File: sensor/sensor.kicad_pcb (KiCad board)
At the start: 2 copper layers, 34 x 34 mm, 17 parts

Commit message: Thubmstick v1
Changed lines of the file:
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@@
       (effects (font (size 1 1) (thickness 0.15)))
     )
-    (fp_rect (start -4.55 -8.1) (end 4.55 8.1) (layer "F.SilkS") (width 0.12) (fill none))
+    (fp_rect (start -4.55 -8.1) (end 4.55 8.1) (layer "Edge.Cuts") (width 0.12) (fill none))
     (pad "1" thru_hole circle (at -5.35 -6.58) (size 1.2 1.2) (drill 0.7) (layers *.Cu *.Mask)
       (net 11 "unconnected-(SN1-Pad1)") (pinfunction "NC") (pintype "input+no_connect"))
@@
     (pad "16" thru_hole circle (at 5.35 -5.69) (size 1.2 1.2) (drill 0.7) (layers *.Cu *.Mask)
       (net 17 "unconnected-(SN1-Pad16)") (pinfunction "NC") (pintype "input+no_connect"))
-    (zone (net 0) (net_name "") (layer "F.SilkS") (hatch edge 0.508)
-      (connect_pads (clearance 0))
-      (min_thickness 0.254)
-      (keepout (tracks not_allowed) (vias not_allowed) (pads not_allowed ) (copperpour allowed) (footprints allowed))
-      (fill (thermal_gap 0.508) (thermal_bridge_width 0.508))
-      (polygon
-        (pts
-          (xy 154.55 108.1)
-          (xy 145.45 108.1)
-          (xy 145.45 91.9)
-          (xy 154.55 91.9)
-        )
-      )
-    )
   )
   (footprint "Capacitor_SMD:C_0603_1608Metric" (layer "F.Cu")

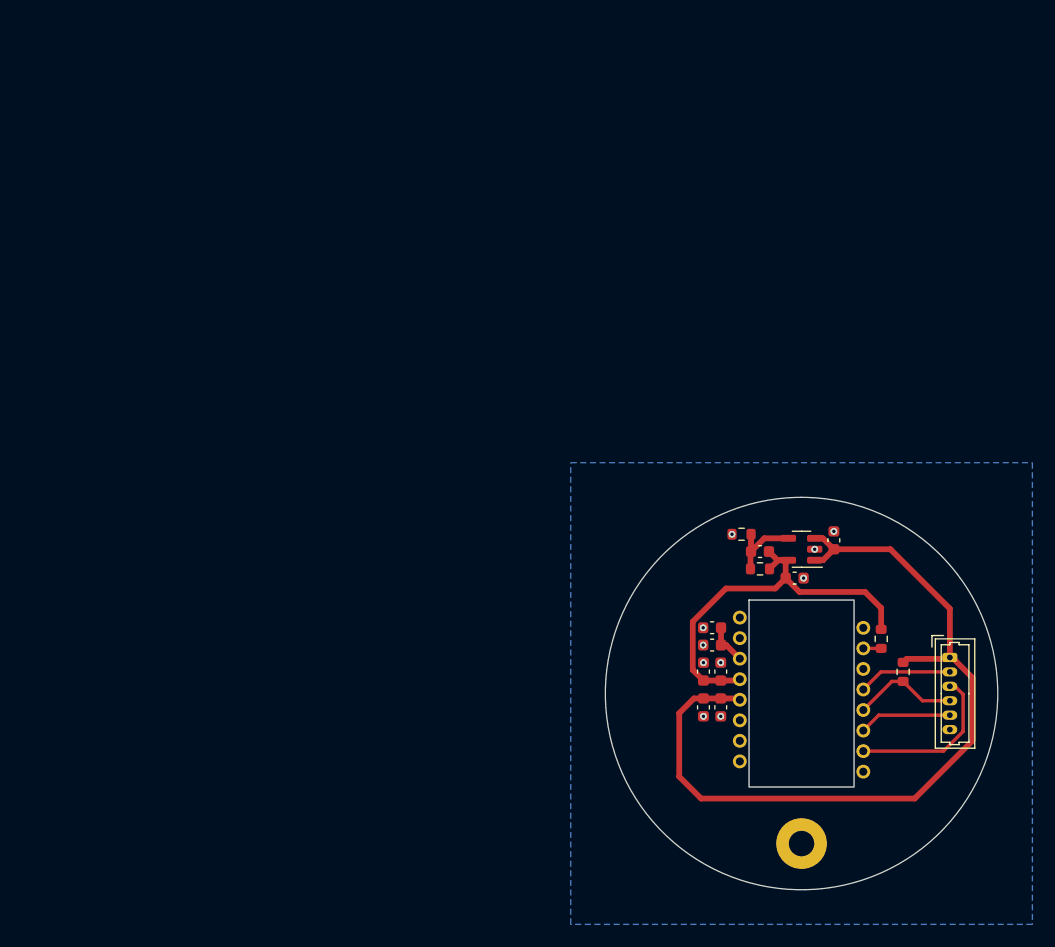
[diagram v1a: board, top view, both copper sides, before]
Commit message: update sensor and stick, add trigger project
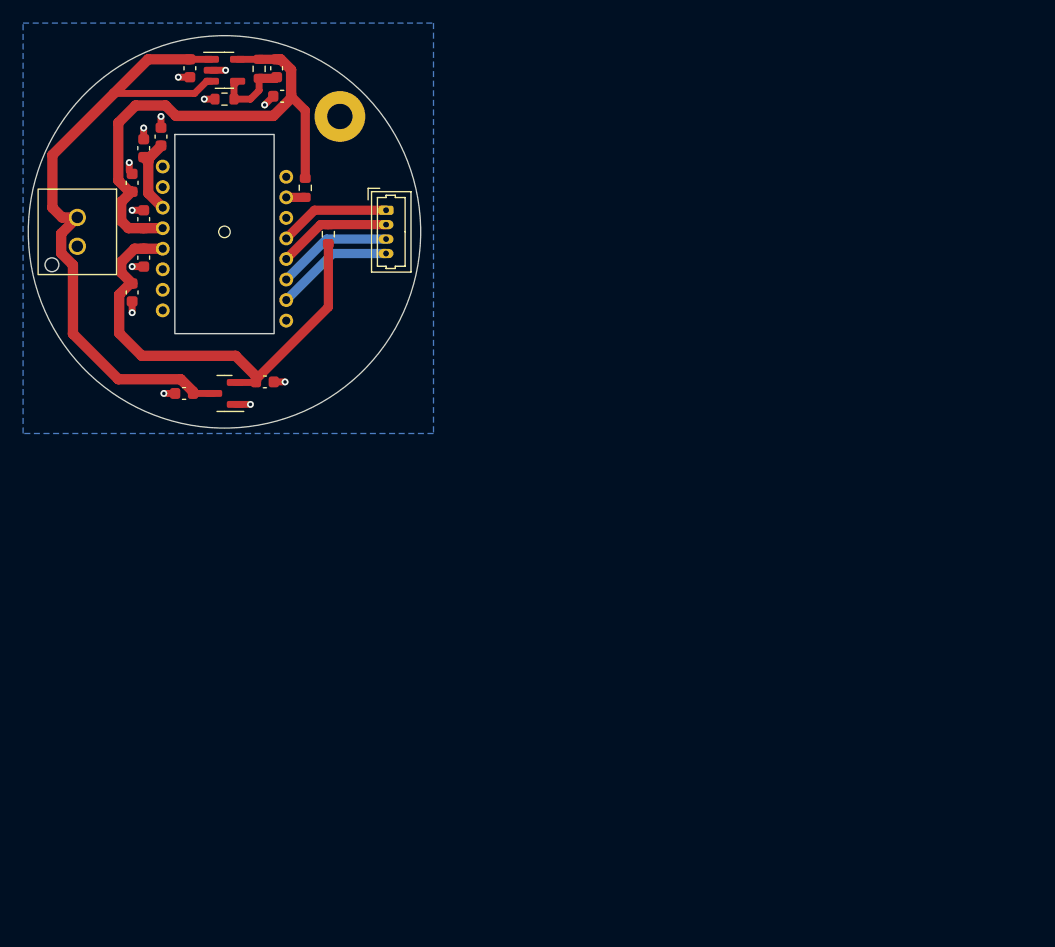
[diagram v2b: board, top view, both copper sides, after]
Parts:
- removed C1: 10uF, Capacitor_SMD:C_0603_1608Metric
- removed LDO1: AP2127K-ADJ, Package_TO_SOT_SMD:SOT-23-5
- removed MNT1: MountingHole, MountingHole:MountingHole_2.2mm_M2_Pad
- removed SN1: PMW3360DM-T2QU, PixArt:PMW3360DM-T2QU
- added C10: 4.7u, Capacitor_SMD:C_0603_1608Metric, F.Cu at (94.5, 51.8)
- added C11: 100n, Capacitor_SMD:C_0603_1608Metric, F.Cu at (93.0, 52.8)
- added Ce: 10u, Capacitor_SMD:C_0603_1608Metric, F.Cu at (97.0, 45.8)
- added J1: Conn_01x02, klib:MOLEX_533750210-Mini-Lock-2Pin-Through-Hole, F.Cu at (87.2, 60.0)
- added J2: Conn_01x04, Connector_Molex:Molex_PicoBlade_53047-0410_1x04_P1.25mm_Vertical, F.Cu at (114.0, 58.1)
- added U1: AP2127K-ADJ, Package_TO_SOT_SMD:SOT-23-5, F.Cu at (100.0, 46.0)
- added U2: AP2127N-3.3, Package_TO_SOT_SMD:SOT-23, F.Cu at (100.0, 74.0)
- added U3: PMW3360DM-T2QU, PixArt:PMW3360DM-T2QU, F.Cu at (100.0, 60.0)
- C2: value 1.3pF -> 1.4n
- C3, C4, C6: value 10uF -> 10u
- C5: value 100nF -> 10u
- C7, C9: value 100nF -> 100n
- C8: value 4.7uF -> 10u
- H1: value Conn_01x06 -> MountingHole; footprint Connector_Molex:Molex_PicoBlade_53047-0610_1x06_P1.25mm_Vertical -> MountingHole:MountingHole_2.2mm_M2_Pad
- R1: value 15KR -> 15k
- R2: value 10KR -> 10k
- R3: value 39R -> 39
- R4: value 10KR -> 10K
- moved H1 70.6 mm to (110.0, 50.0), turned to 0 degrees
- moved C6 67.2 mm to (92.0, 55.8), turned to 90 degrees
- moved C7 65.5 mm to (93.0, 58.9), turned to 90 degrees
- moved R3 63.4 mm to (107.0, 56.2), turned to -90 degrees
- moved R4 62.6 mm to (109.0, 60.2)
- moved R1 61.3 mm to (103.0, 45.9), turned to -90 degrees
- moved C3 60.9 mm to (105.0, 48.2), turned to 180 degrees
- moved C9 59.6 mm to (93.0, 62.2), turned to -90 degrees
- moved C2 59.2 mm to (104.5, 45.8), turned to -90 degrees
- moved R2 58.6 mm to (100.0, 48.5)
- moved C8 58.0 mm to (92.0, 65.2), turned to -90 degrees
- moved C4 51.0 mm to (96.5, 74.0), turned to 180 degrees
- moved C5 46.8 mm to (103.5, 73.0), turned to 0 degrees
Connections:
- C2 pad 1: VDD -> 2V
- C3 pad 1: VDD -> 2V
- C4 pad 1: VDD -> 5V
- C5 pad 1: VDD -> 3V3
- C6 pad 1: VDDIO -> 2V
- C7 pad 1: VDDIO -> 2V
- C8 pad 1: VDDPIX -> 3V3
- C9 pad 1: VDDPIX -> 3V3
- H1 pad 1: VDDIO -> (no net)
- R1 pad 1: VDD -> 2V
- R3 pad 1: LED_P -> 2V
- R3 pad 2: VDD -> LED_P
- R4 pad 1: MISO -> 3V3
- R4 pad 2: VDDIO -> MISO
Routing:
- net VDDIO: track 72.5 -> 0.00 mm
- net 5V: track 0.00 -> 58.7 mm
- net 2V: track 0.00 -> 45.1 mm
- net 3V3: track 0.00 -> 41.6 mm
- net VDD: track 35.1 -> 0.00 mm
- net GND: track 0.00 -> 13.5 mm, vias 10 -> 13
- net SCLK: track 14.0 -> 10.3 mm
- net VDDPIX: track 3.61 -> 7.00 mm
- net MOSI: track 8.05 -> 10.1 mm
- net NCS: track 8.13 -> 9.66 mm
- net MISO: track 9.22 -> 9.88 mm
